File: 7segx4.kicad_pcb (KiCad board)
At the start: 2 copper layers, 203.2 x 86.4 mm, 5 parts, among them x1 HEADER2X7

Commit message: track width+
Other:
- net class Default: trace_width 1.016 -> 1.524

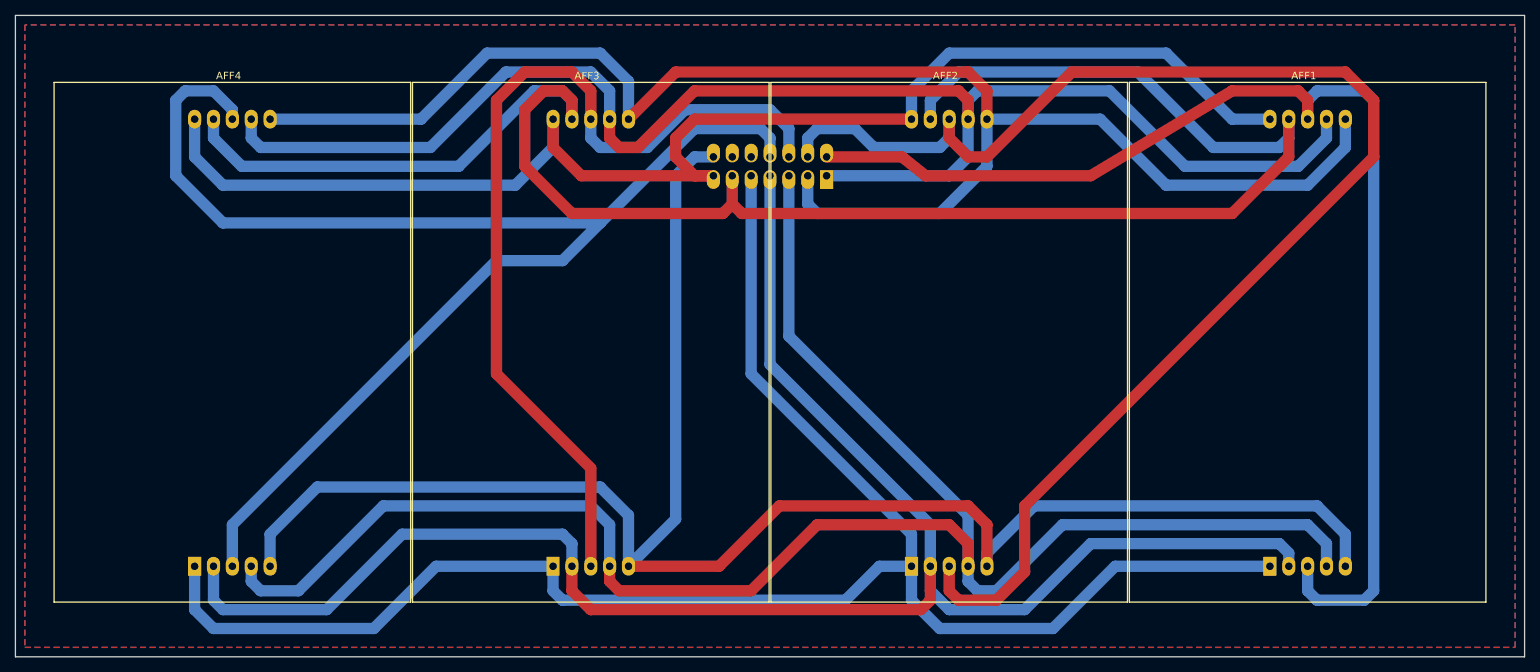
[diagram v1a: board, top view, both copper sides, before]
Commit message: size changed
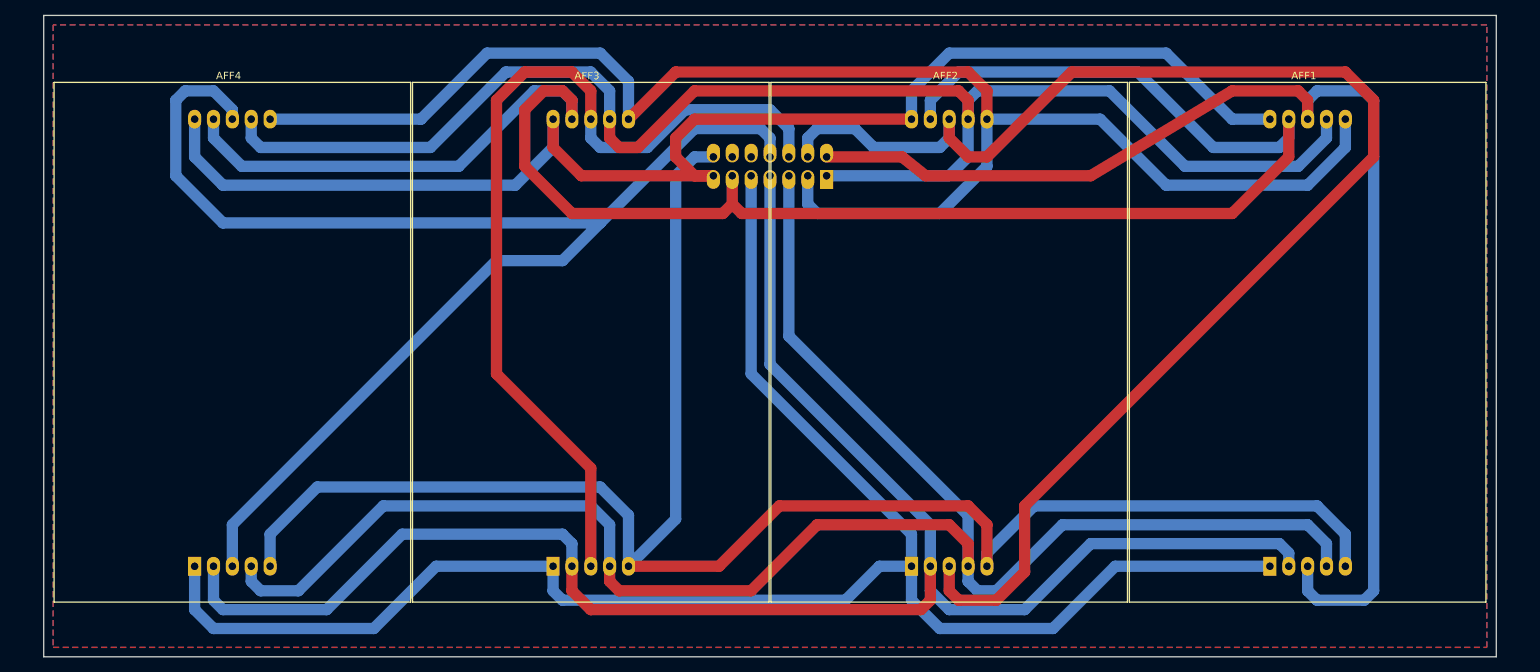
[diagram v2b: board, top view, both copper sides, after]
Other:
- board size 203.2 x 86.4 mm -> 195.6 x 86.4 mm
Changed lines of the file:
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@@
     (links 40)
     (no_connects 0)
-    (area 35.484999 21.514999 238.835001 108.025001)
+    (area 36.83 21.514999 237.490001 108.025001)
     (thickness 1.6)
     (drawings 5)
@@
     (15 F.Cu signal)
     (0 B.Cu signal)
-    (16 B.Adhes user)
-    (17 F.Adhes user)
-    (18 B.Paste user)
-    (19 F.Paste user)
-    (20 B.SilkS user)
+    (16 B.Adhes user hide)
+    (17 F.Adhes user hide)
+    (18 B.Paste user hide)
+    (19 F.Paste user hide)
+    (20 B.SilkS user hide)
     (21 F.SilkS user)
-    (22 B.Mask user)
-    (23 F.Mask user)
-    (24 Dwgs.User user)
-    (25 Cmts.User user)
-    (26 Eco1.User user)
-    (27 Eco2.User user)
+    (22 B.Mask user hide)
+    (23 F.Mask user hide)
+    (24 Dwgs.User user hide)
+    (25 Cmts.User user hide)
+    (26 Eco1.User user hide)
+    (27 Eco2.User user hide)
     (28 Edge.Cuts user)
   )
@@
       (layerselection 283148289)
       (usegerberextensions true)
-      (excludeedgelayer false)
+      (excludeedgelayer true)
       (linewidth 0.150000)
       (plotframeref true)
@@
     )
   )
-  (gr_line (start 238.76 107.95) (end 238.76 21.59) (angle 90) (layer Edge.Cuts) (width 0.15))
-  (gr_line (start 35.56 107.95) (end 35.56 21.59) (angle 90) (layer Edge.Cuts) (width 0.15))
-  (gr_line (start 238.76 107.95) (end 35.56 107.95) (angle 90) (layer Edge.Cuts) (width 0.15))
-  (gr_line (start 35.56 21.59) (end 238.76 21.59) (angle 90) (layer Edge.Cuts) (width 0.15))
+  (gr_line (start 234.95 107.95) (end 234.95 21.59) (angle 90) (layer Edge.Cuts) (width 0.15))
+  (gr_line (start 39.37 107.95) (end 39.37 21.59) (angle 90) (layer Edge.Cuts) (width 0.15))
+  (gr_line (start 234.95 107.95) (end 39.37 107.95) (angle 90) (layer Edge.Cuts) (width 0.15))
+  (gr_line (start 39.37 21.59) (end 234.95 21.59) (angle 90) (layer Edge.Cuts) (width 0.15))
   (target plus (at 46.99 91.44) (size 0.005) (width 0.15) (layer Edge.Cuts))
   (segment (start 144.78 43.18) (end 161.29 43.18) (width 1.524) (layer B.Cu) (net 1) (status 10))
@@
     (polygon
       (pts
-        (xy 36.83 106.68) (xy 237.49 106.68) (xy 237.49 22.86) (xy 36.83 22.86)
+        (xy 40.64 106.68) (xy 233.68 106.68) (xy 233.68 22.86) (xy 40.64 22.86)
       )
     )
@@
     (polygon
       (pts
-        (xy 36.83 106.68) (xy 237.49 106.68) (xy 237.49 22.86) (xy 36.83 22.86)
+        (xy 40.64 106.68) (xy 233.68 106.68) (xy 233.68 22.86) (xy 40.64 22.86)
       )
     )
